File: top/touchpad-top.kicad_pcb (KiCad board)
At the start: 2 copper layers, 28.3 x 40 mm, 16 parts, among them P1 CONN_10, P2 CONN_5, U1 IQS572, U4 ESD

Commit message: Temporary commit
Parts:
- moved VR1 5.74 mm to (205.3, 136.4), turned to 270 degrees
- moved FB2 4.34 mm to (202.2, 136.4), turned to 90 degrees
- moved C7 3.15 mm to (200.9, 136.4)
- moved C4 1.84 mm to (206.6, 132.6)
- moved C5 1.84 mm to (207.4, 133.4)
- moved C3 1.84 mm to (205.7, 131.7)
- moved C6 1.84 mm to (208.3, 134.2)
- moved C12 1.52 mm to (208.6, 136.6), turned to 270 degrees
- moved C1 0.63 mm to (204.8, 130.9), turned to 45 degrees
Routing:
- net /RDY: track 3.28 -> 40.8 mm
- net /VCC_BOTTOM: track 0.66 -> 25.8 mm
- net /SCL: track 0.00 -> 18.9 mm
- net /SDA: track 2.80 -> 16.6 mm
- net +3V3: track 0.00 -> 10.4 mm
- net /SCL_BOTTOM: track 0.00 -> 7.48 mm
- net /TX5: track 13.7 -> 19.9 mm, vias 1 -> 9
- net /TX1: track 17.1 -> 11.5 mm, vias 13 -> 10
- net /RX5: track 5.72 -> 11.3 mm
- net /TX3: track 2.05 -> 6.84 mm
- net /RX1: track 12.7 -> 17.2 mm
- net /RX0: track 14.8 -> 19.4 mm
- net /SDA_BOTTOM: track 0.00 -> 4.53 mm
- net +5V: track 0.00 -> 4.42 mm
- net /RX4: track 3.43 -> 7.71 mm, vias 1 -> 2
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
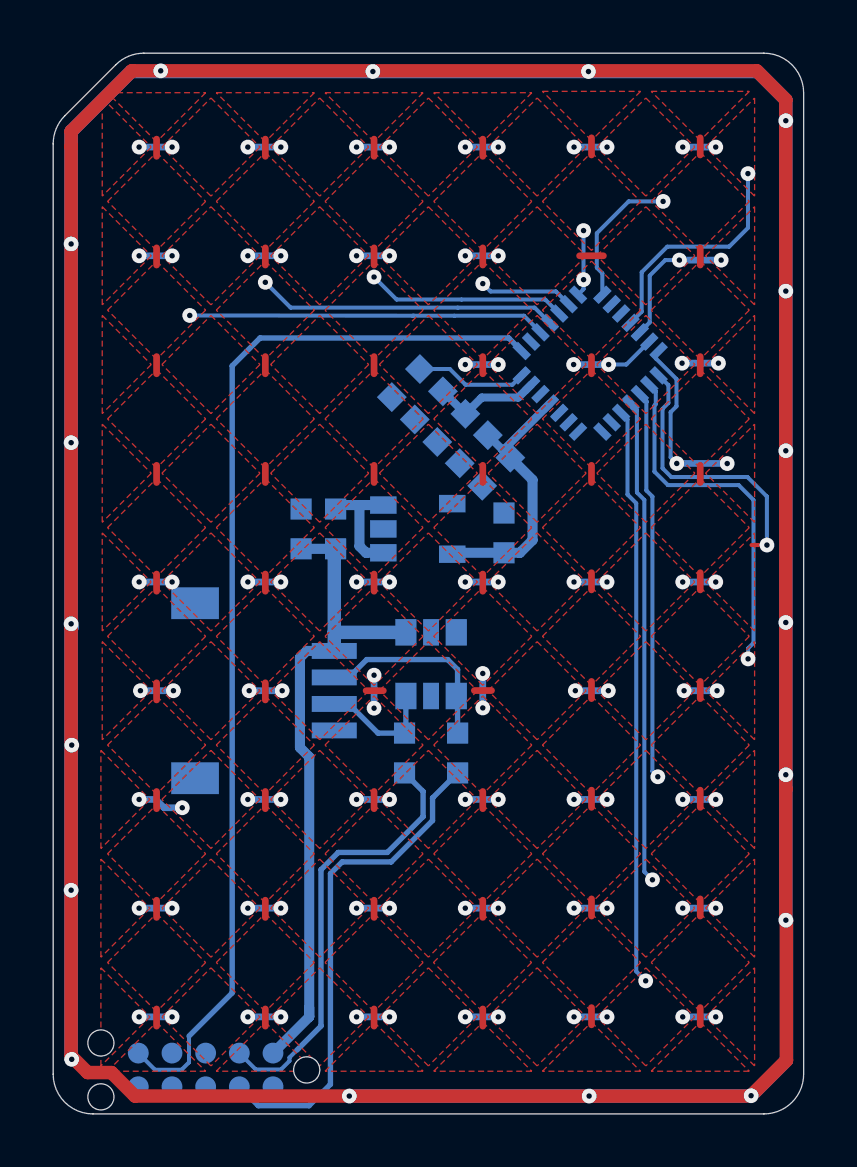
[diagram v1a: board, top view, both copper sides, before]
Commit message: Add GND zone.
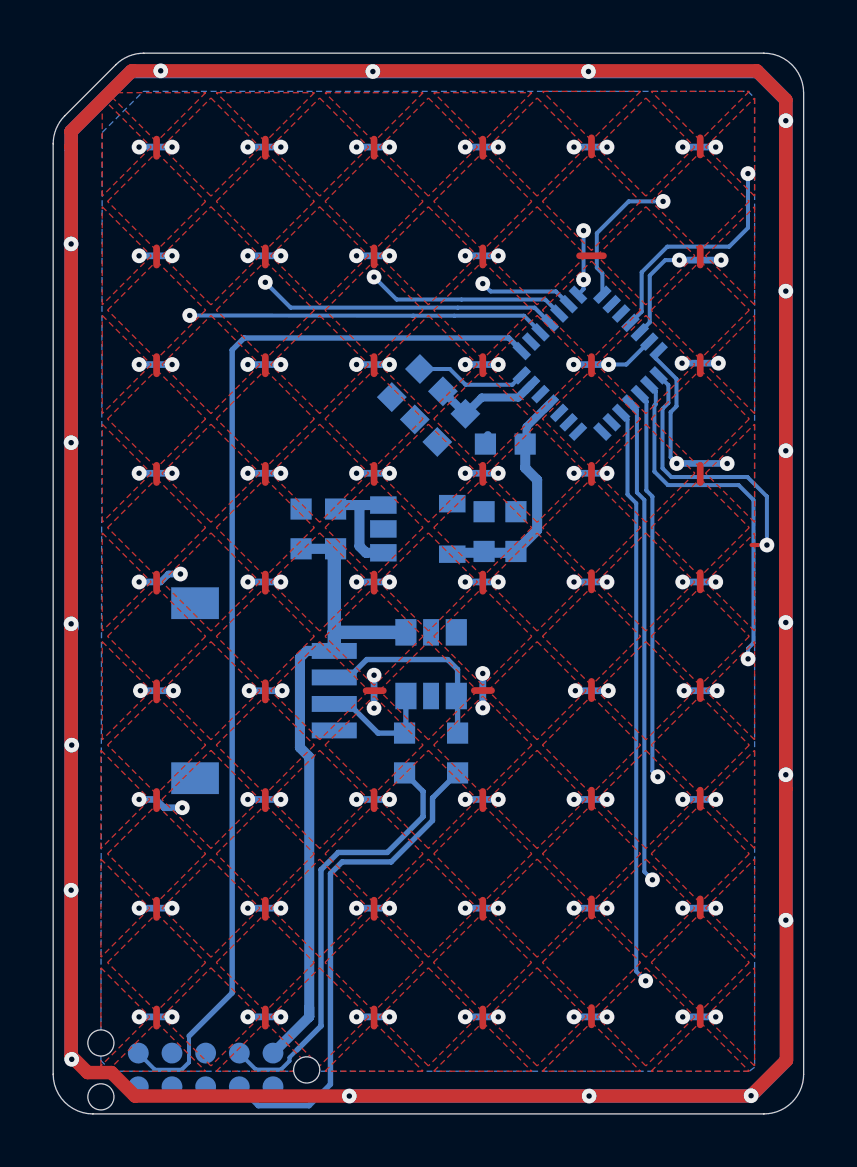
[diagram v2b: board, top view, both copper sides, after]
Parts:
- moved C6 2.38 mm to (209.0, 136.5), turned to 270 degrees
- moved C5 1.21 mm to (208.6, 133.2), turned to 0 degrees
- moved C12 0.75 mm to (207.8, 136.5)
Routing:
- net /TX3: track 6.84 -> 13.1 mm, vias 2 -> 12
- net /TX2: track 5.83 -> 9.56 mm, vias 6 -> 12
- net /TX4: track 15.5 -> 18.4 mm, vias 8 -> 13
- net (no net): track 2.49 -> 0.00 mm, vias 5 -> 0
- net +3V3: track 10.4 -> 8.68 mm
- added copper zone on B.Cu, net GND

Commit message: Final routing.
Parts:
- added C2: 1uF, UGL:SM0603, B.Cu at (201.5, 133.2)
- added C8: 0.1uF, UGL:SM0603, B.Cu at (201.5, 132.0)
- moved P1 17.9 mm to (209.8, 144.0), turned to 270 degrees
- moved R7 1.76 mm to (206.5, 145.3), turned to 180 degrees
- moved R6 0.81 mm to (206.5, 144.1), turned to 180 degrees
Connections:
- net /PGM renamed Net-(U1-Pad27)
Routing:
- net GND: track 244.3 -> 278.3 mm, vias 18 -> 19
- net /RDY: track 41.1 -> 20.6 mm, vias 0 -> 2
- net /VCC_BOTTOM: track 25.8 -> 12.9 mm
- net /RX4: track 7.71 -> 11.4 mm, vias 2 -> 8
- net +5V: track 4.42 -> 8.11 mm
- net /SDA_BOTTOM: track 4.53 -> 7.82 mm
- net /SDA: track 16.6 -> 19.6 mm
- net /SCL: track 18.9 -> 16.6 mm
- net /TX3: track 13.1 -> 12.5 mm, vias 12 -> 10
- net /TX4: track 18.4 -> 18.0 mm, vias 13 -> 11
- net /TX5: track 19.9 -> 19.5 mm, vias 9 -> 7

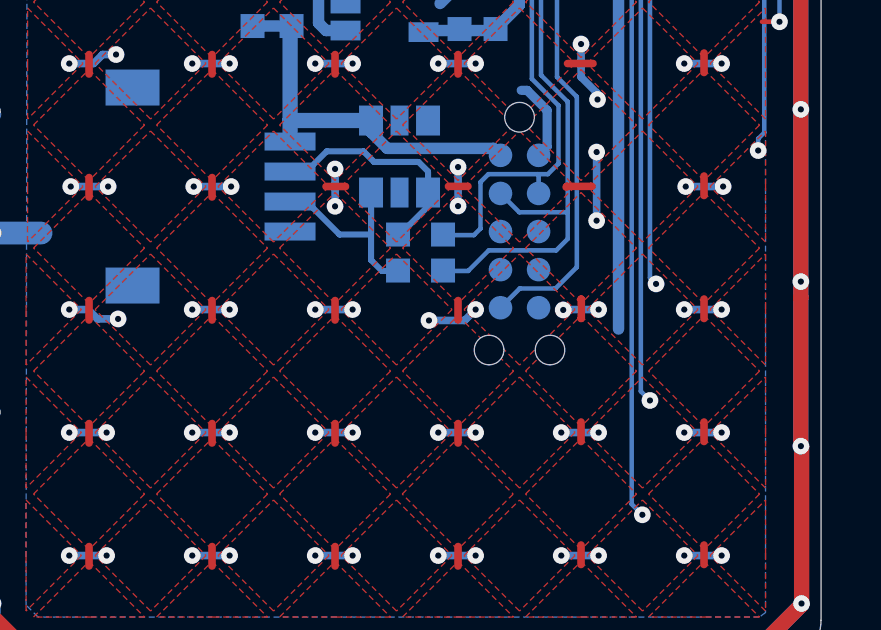
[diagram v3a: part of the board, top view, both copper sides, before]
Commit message: Finish silkscreen and increase version number.
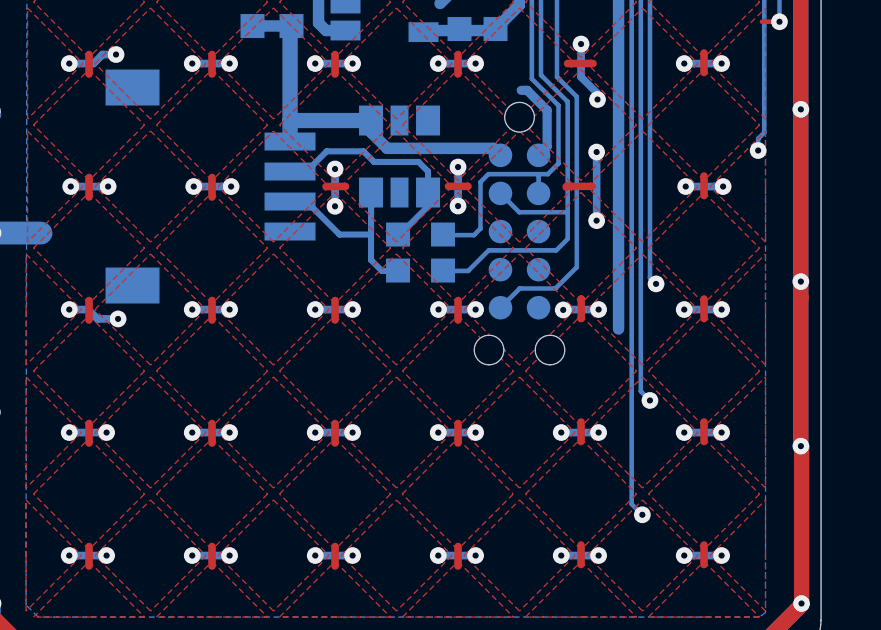
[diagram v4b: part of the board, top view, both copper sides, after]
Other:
- board text added: "PCB_ID: touchpad_top_2.4.0"
- board text removed: "PCB_ID: touchpad_top_2.3.0"

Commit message: Bump version to 3.0.0 and tidy up silk screen a bit.
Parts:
- moved G*** 0.90 mm to (205.2, 124.1)
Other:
- board text added: "PCB_ID: touchpad_top_3.0.0"
- board text removed: "PCB_ID: touchpad_top_2.4.0"

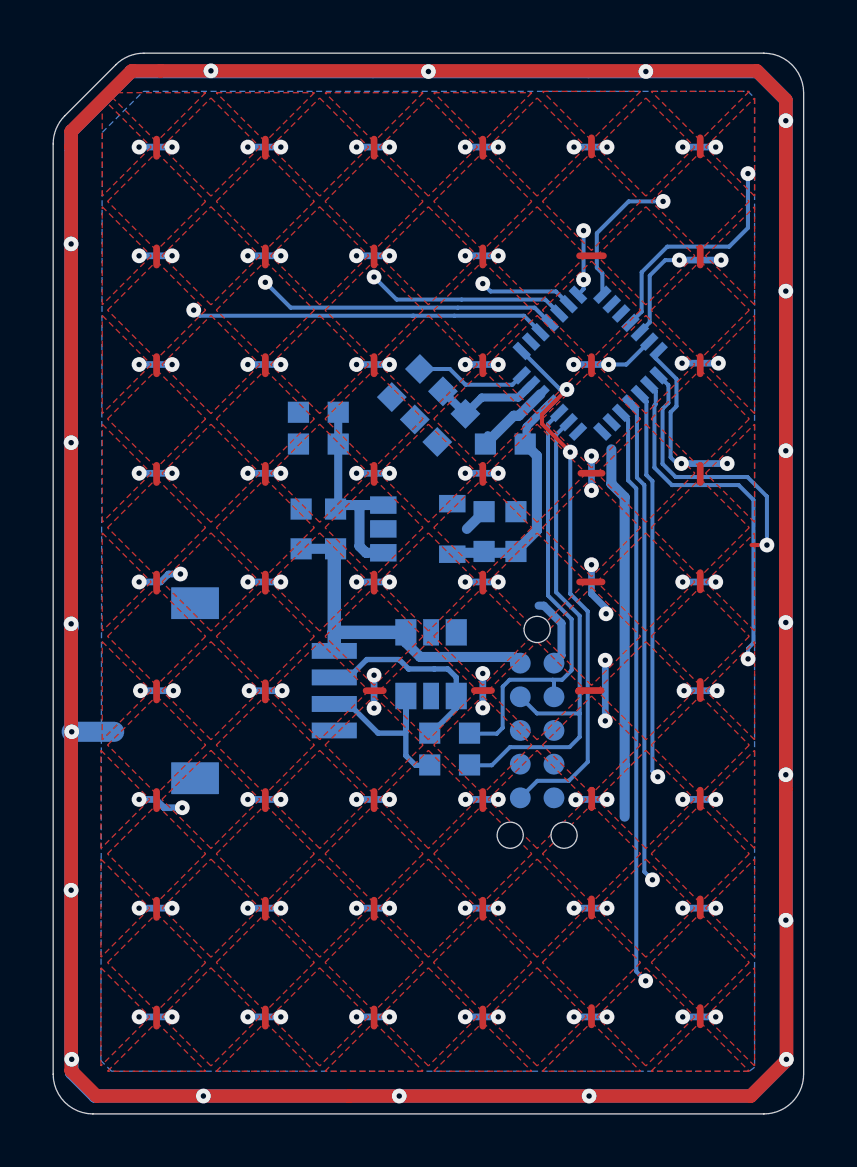
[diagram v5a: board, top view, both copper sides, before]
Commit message: New sensor grid. (0.15mm sensor gap)
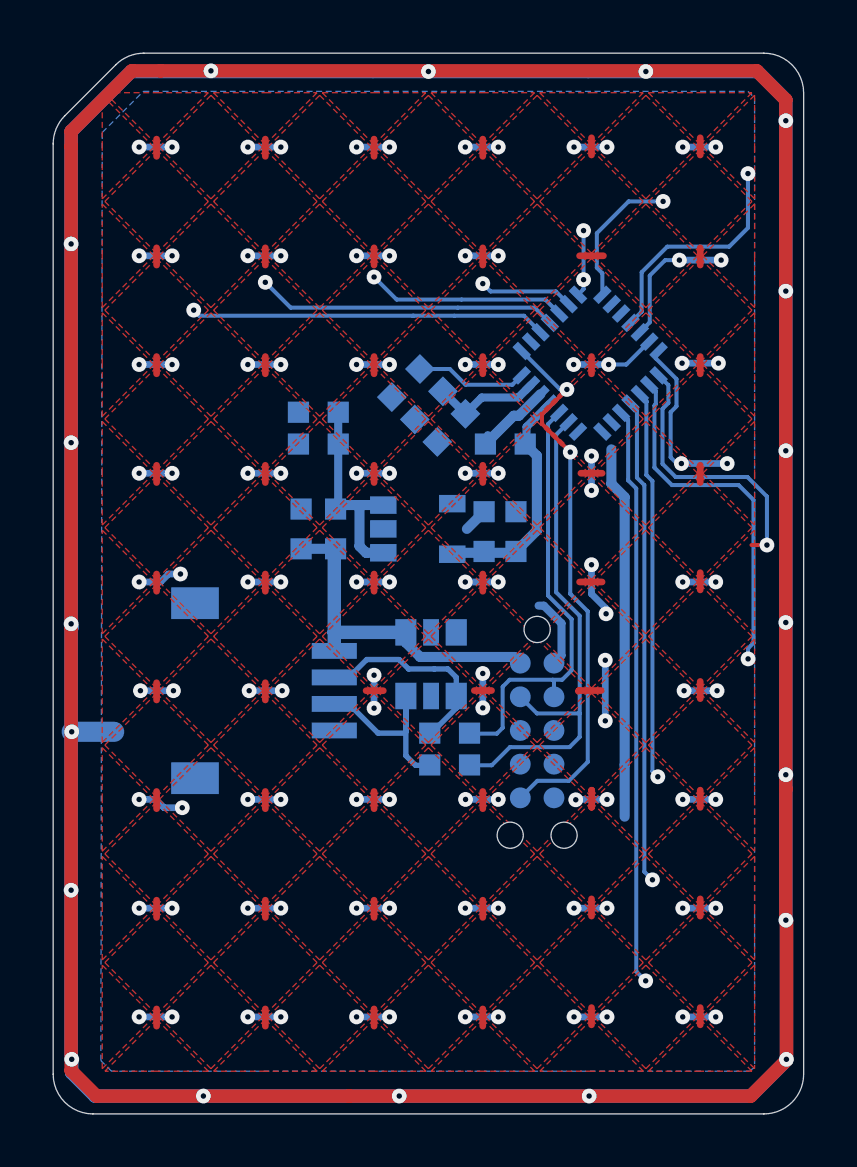
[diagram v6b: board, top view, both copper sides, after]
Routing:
- net /TX6: track 22.6 -> 23.9 mm
- net /RX5: track 11.3 -> 9.95 mm
- added copper zone on F.Cu, net (none)
- removed copper zone on F.Cu, net /RX0
- removed copper zone on F.Cu, net /RX1
- removed copper zone on F.Cu, net /RX2
- removed copper zone on F.Cu, net /RX3
- removed copper zone on F.Cu, net /RX4
- removed copper zone on F.Cu, net /RX5
- removed copper zone on F.Cu, net /TX0
- removed copper zone on F.Cu, net /TX1
- removed copper zone on F.Cu, net /TX2
- removed copper zone on F.Cu, net /TX3
- removed copper zone on F.Cu, net /TX4
- removed copper zone on F.Cu, net /TX5
- removed copper zone on F.Cu, net /TX6
- removed copper zone on F.Cu, net /TX7
- removed copper zone on F.Cu, net /TX8

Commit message: Reconnect all sensors.
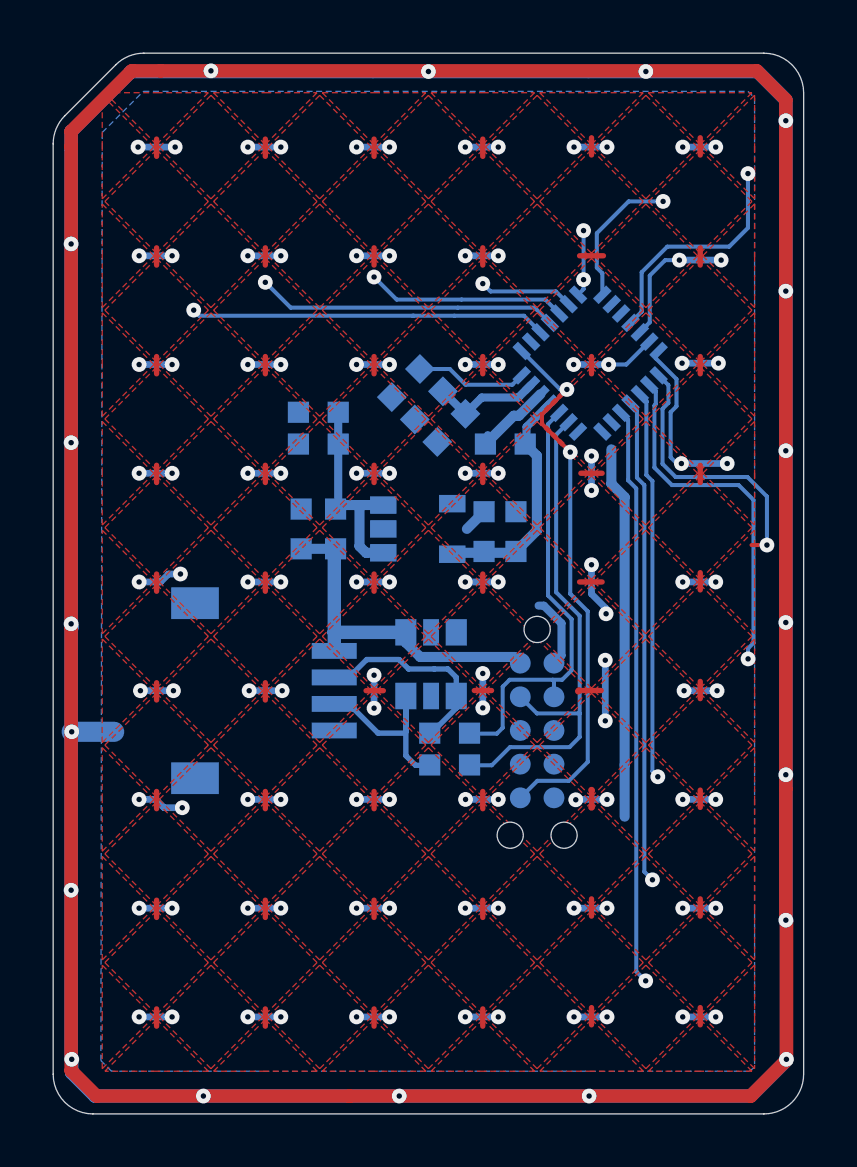
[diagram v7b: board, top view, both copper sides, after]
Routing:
- net /TX6: track 23.9 -> 22.6 mm
- net /RX5: track 9.95 -> 11.3 mm
- added copper zone on F.Cu, net /RX0
- added copper zone on F.Cu, net /RX1
- added copper zone on F.Cu, net /RX2
- added copper zone on F.Cu, net /RX3
- added copper zone on F.Cu, net /RX4
- added copper zone on F.Cu, net /RX5
- added copper zone on F.Cu, net /TX0
- added copper zone on F.Cu, net /TX1
- added copper zone on F.Cu, net /TX2
- added copper zone on F.Cu, net /TX3
- added copper zone on F.Cu, net /TX4
- added copper zone on F.Cu, net /TX5
- added copper zone on F.Cu, net /TX6
- added copper zone on F.Cu, net /TX7
- added copper zone on F.Cu, net /TX8
- removed copper zone on F.Cu, net (none)
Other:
- net class Default: clearance 0.1524 -> 0.0762
- rule trace_clearance: 0.1524 -> 0.0762
